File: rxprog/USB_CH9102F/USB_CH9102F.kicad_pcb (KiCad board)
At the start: 2 copper layers, 69 x 29 mm, 20 parts, among them J1 5077CR-16-SMC2-BK-TR, J2 USB-C OPT, J3 Serial In/Out Full, J4 GPIO, J5 SUSPEND, J6 /SUSPEND, J7 /ACT, J8 /RST, J9 Serial In/Out, SW1 3P-SW, U1 CH9102F, U2 NJU7223DL1-33

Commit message: Update: track
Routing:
- net GND: track 35.6 -> 32.9 mm, vias 10 -> 44
- net Net-(J1-SBU2): track 22.8 -> 20.4 mm, vias 0 -> 2
- net //DTR: track 49.3 -> 51.2 mm, vias 1 -> 2
- net //DSR: track 44.6 -> 46.4 mm, vias 1 -> 2
- net Net-(J1-CC1): track 12.8 -> 11.6 mm, vias 0 -> 1
- net Net-(U1-D+): track 11.2 -> 12.3 mm
- net //RTS: track 47.8 -> 48.6 mm, vias 1 -> 2
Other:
- board text added: "CH9102F USB/Serial"

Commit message: Update: add USB/Register, LED
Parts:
- added D2: RED, LED_SMD:LED_0603_1608Metric_Pad1.05x0.95mm_HandSolder, F.Cu at (116.0, 87.4)
- added D3: RED, LED_SMD:LED_0603_1608Metric_Pad1.05x0.95mm_HandSolder, F.Cu at (116.0, 89.9)
- added R2: 10K, Resistor_SMD:R_0603_1608Metric_Pad0.98x0.95mm_HandSolder, F.Cu at (100.3, 102.5)
- added R3: 10K, Resistor_SMD:R_0603_1608Metric_Pad0.98x0.95mm_HandSolder, F.Cu at (98.2, 102.5)
- added R4: 2K, Resistor_SMD:R_0603_1608Metric_Pad0.98x0.95mm_HandSolder, F.Cu at (119.5, 87.4)
- added R5: 2K, Resistor_SMD:R_0603_1608Metric_Pad0.98x0.95mm_HandSolder, F.Cu at (119.5, 89.9)
- J2: value USB-C OPT -> USB/OPT; footprint Connector_PinHeader_2.54mm:PinHeader_1x04_P2.54mm_Vertical -> Connector_PinHeader_2.54mm:PinHeader_1x02_P2.54mm_Vertical
- moved J2 5.08 mm to (104.3, 102.6)
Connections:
- J2 pad 1: Net-(J1-CC1) -> Net-(J1-SBU1)
- J2 pad 2: Net-(J1-CC2) -> Net-(J1-SBU2)
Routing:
- net Net-(D2-A): track 90.0 -> 106.5 mm, vias 0 -> 3
- net GND: track 32.9 -> 40.6 mm
- net Net-(J4-Pin_1): track 22.0 -> 26.3 mm
- net Net-(J4-Pin_2): track 20.5 -> 24.6 mm
- net Net-(J1-SBU2): track 20.4 -> 17.7 mm
- net Net-(J1-CC2): track 8.35 -> 5.82 mm
- net Net-(D3-K): track 0.00 -> 1.73 mm
- net Net-(D2-K): track 0.00 -> 1.73 mm
- net Net-(J1-SBU1): track 10.8 -> 12.5 mm
- net Net-(J1-CC1): track 11.6 -> 10.7 mm, vias 1 -> 2
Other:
- board text removed: "CC1"
- board text removed: "CC2"

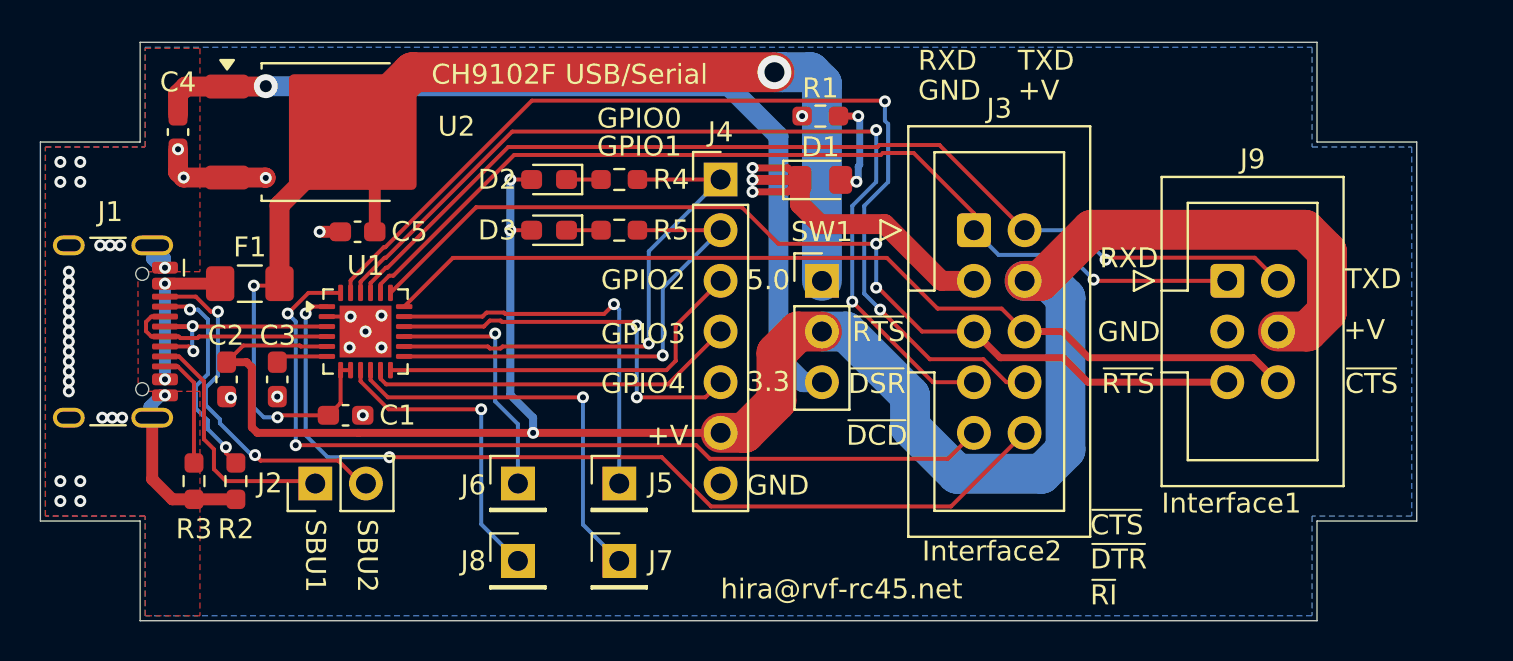
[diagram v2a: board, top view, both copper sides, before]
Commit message: Update: CC1 pull down register
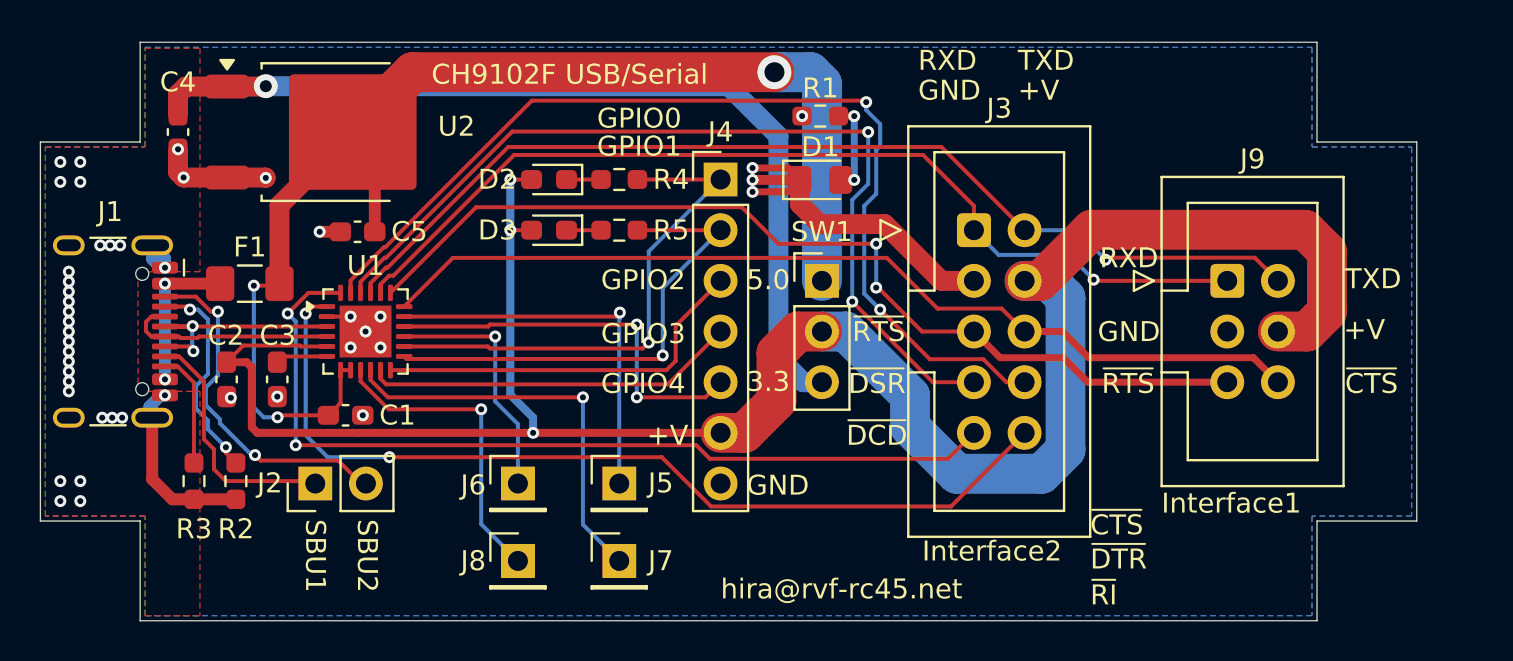
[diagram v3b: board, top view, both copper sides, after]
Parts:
- R2, R3: value 10K -> 5.1K
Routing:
- net //DTR: track 51.2 -> 50.3 mm
- net //DSR: track 46.4 -> 45.7 mm
- net Net-(D1-A): track 5.20 -> 4.66 mm
